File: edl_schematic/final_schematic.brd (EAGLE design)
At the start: 329.6 x 243.8 mm, 296 parts, among them IC1 FT232RL, IC14 TL084D, IC15 TL084D, IC16 TL084D, IC17 TL084D, IC18 TL084D, IC19 TL084D, IC20 TL084D, IC21 TL084D, IC22 TL084D, IC23 TL084D, IC24 TL084D, IC25 TL084D, IC26 TL084D, IC27 TL084D, IC28 TL084D, IC29 TL084D, IC3 TL084D, IC30 TL084D, IC4 TPS77333, IC5 TL084D, IC6 7812TV, Q1 BC558B, U1 TMS320F28069_PN_80, U3 TLV5610_DW_20, U4 MAX395EWG, U6 MAX395EWG, U7 MAX395EWG, X1 USB

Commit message: USB_UPDATED
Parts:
- removed X1: USB, con-berg:PN61729
- added CON1: UBC05V128-B0C04D, con-cypressindustries:32005-201
- added F1: 500mA, rcl:L1812
- added R19: 0, rcl:R1206
- added R20: 0, rcl:R1206W
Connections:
- new net N$12: CON1.2, R19.1
- new net N$13: CON1.3, R20.1
- new net XUSB: CON1.1, F1.2
- net GND: now also CON1.5; no longer X1.4
- net USBDM: now also R19.2; no longer X1.2
- net USBDP: now also R20.2; no longer X1.3
- net VBUS: now also F1.1; no longer X1.1
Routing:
- net USBDM: track 68.6 -> 89.6 mm, vias 0 -> 1
- net USBDP: track 78.6 -> 96.0 mm, vias 0 -> 1
- net N$13: track 0.00 -> 16.8 mm
- net N$12: track 0.00 -> 12.5 mm
- net XUSB: track 0.00 -> 11.5 mm
- net VBUS: track 110.9 -> 115.2 mm
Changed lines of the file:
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@@
 <attribute name="VALUE" x="82.130903125" y="62.0903" size="1.27" layer="27" rot="R270"/>
 </element>
-<element name="X1" library="con-berg" package="PN61729" value="USB" x="-30.1523375" y="47.800259375" smashed="yes" rot="R270">
-<attribute name="MF" value="" x="-11.694159375" y="63.14948125" size="1.778" layer="27" rot="R270" display="off"/>
-<attribute name="MPN" value="" x="-11.694159375" y="63.14948125" size="1.778" layer="27" rot="R270" display="off"/>
-<attribute name="NAME" x="-23.8023375" y="54.150259375" size="1.27" layer="25" rot="R270"/>
-<attribute name="OC_FARNELL" value="unknown" x="-11.694159375" y="63.14948125" size="1.778" layer="27" rot="R270" display="off"/>
-<attribute name="OC_NEWARK" value="unknown" x="-11.694159375" y="63.14948125" size="1.778" layer="27" rot="R270" display="off"/>
-<attribute name="VALUE" x="-39.0423375" y="40.180259375" size="1.27" layer="27"/>
+<element name="CON1" library="con-cypressindustries" package="32005-201" value="UBC05V128-B0C04D" x="-25.18155625" y="31.861759375" smashed="yes">
+<attribute name="MF" value="" x="-35.8038375" y="46.898559375" size="1.778" layer="27" display="off"/>
+<attribute name="MPN" value="" x="-35.8038375" y="46.898559375" size="1.778" layer="27" display="off"/>
+<attribute name="NAME" x="-29.62655625" y="37.576759375" size="1.27" layer="25"/>
+<attribute name="OC_FARNELL" value="unknown" x="-35.8038375" y="46.898559375" size="1.778" layer="27" display="off"/>
+<attribute name="OC_NEWARK" value="unknown" x="-35.8038375" y="46.898559375" size="1.778" layer="27" display="off"/>
+<attribute name="VALUE" x="-29.62655625" y="24.876759375" size="1.27" layer="27"/>
+</element>
+<element name="F1" library="rcl" package="L1812" value="500mA" x="-11.932921875" y="36.3245375" smashed="yes" rot="R180">
+<attribute name="NAME" x="-10.027921875" y="34.4195375" size="1.27" layer="25" rot="R180"/>
+<attribute name="VALUE" x="-10.027921875" y="39.4995375" size="1.27" layer="27" rot="R180"/>
+</element>
+<element name="R19" library="rcl" package="R1206" value="0" x="-11.8516375" y="29.05251875" smashed="yes">
+<attribute name="NAME" x="-13.1216375" y="30.32251875" size="1.27" layer="25"/>
+<attribute name="VALUE" x="-13.1216375" y="26.51251875" size="1.27" layer="27"/>
+</element>
+<element name="R20" library="rcl" package="R1206W" value="0" x="-12.26311875" y="22.4028" smashed="yes">
+<attribute name="NAME" x="-14.16811875" y="23.6728" size="1.27" layer="25"/>
+<attribute name="VALUE" x="-14.16811875" y="19.8628" size="1.27" layer="27"/>
 </element>
 </elements>
@@
 <wire x1="17.7317375" y1="-42.367203125" x2="17.548859375" y2="-42.55008125" width="0.254" layer="1"/>
 <wire x1="11.793221875" y1="-80.39608125" x2="11.625578125" y2="-80.39608125" width="0.254" layer="1"/>
-<contactref element="X1" pad="4"/>
+<contactref element="CON1" pad="5"/>
 </signal>
 <signal name="VCC" class="1">
@@
 <contactref element="JP6" pad="1"/>
 <via x="1.457959375" y="60.03798125" extent="1-16" drill="0.35"/>
-<wire x1="5.255259375" y1="73.484740625" x2="5.255259375" y2="69.3521625" width="0.4064" layer="1"/>
+<wire x1="5.255259375" y1="73.484740625" x2="5.255259375" y2="71.224140625" width="0.4064" layer="1"/>
+<wire x1="5.255259375" y1="71.224140625" x2="5.255259375" y2="69.3521625" width="0.4064" layer="1"/>
 <wire x1="5.255259375" y1="69.3521625" x2="1.457959375" y2="65.5548625" width="0.4064" layer="1"/>
 <wire x1="1.457959375" y1="60.03798125" x2="1.457959375" y2="65.5548625" width="0.4064" layer="1"/>
 <wire x1="5.255259375" y1="73.484740625" x2="5.08" y2="73.66" width="0.4064" layer="1"/>
-<contactref element="X1" pad="1"/>
-<wire x1="13.84" y1="53.34" x2="12.23518125" y2="53.34" width="0.4064" layer="16"/>
-<wire x1="12.23518125" y1="53.34" x2="8.69188125" y2="56.8833" width="0.4064" layer="16"/>
-<wire x1="8.69188125" y1="56.8833" x2="-8.3972375" y2="56.8833" width="0.4064" layer="16"/>
-<wire x1="-8.3972375" y1="56.8833" x2="-18.80361875" y2="46.47691875" width="0.4064" layer="16"/>
-<wire x1="-18.80361875" y1="46.47691875" x2="-25.368996875" y2="46.47691875" width="0.4064" layer="16"/>
-<wire x1="-25.368996875" y1="46.47691875" x2="-25.4423375" y2="46.550259375" width="0.4064" layer="16"/>
 <wire x1="13.84" y1="57.15" x2="13.218159375" y2="57.15" width="0.4064" layer="16"/>
 <wire x1="10.330178125" y1="60.03798125" x2="1.457959375" y2="60.03798125" width="0.4064" layer="16"/>
 <wire x1="13.218159375" y1="57.15" x2="10.330178125" y2="60.03798125" width="0.4064" layer="16"/>
+<contactref element="F1" pad="1"/>
+<wire x1="-9.982921875" y1="36.3245375" x2="-9.982921875" y2="64.96884375" width="0.4064" layer="1"/>
+<wire x1="-9.982921875" y1="64.96884375" x2="-10.005059375" y2="64.99098125" width="0.4064" layer="1"/>
+<wire x1="-9.982921875" y1="64.96884375" x2="-9.982921875" y2="69.836578125" width="0.4064" layer="1"/>
+<wire x1="-8.595359375" y1="71.224140625" x2="5.255259375" y2="71.224140625" width="0.4064" layer="1"/>
+<wire x1="-9.982921875" y1="69.836578125" x2="-8.595359375" y2="71.224140625" width="0.4064" layer="1"/>
 </signal>
 <signal name="USBDM">
@@
 <wire x1="18.4912" y1="54.71146875" x2="18.4912" y2="51.12445" width="0.4064" layer="16"/>
 <wire x1="18.4912" y1="51.12445" x2="17.428228125" y2="50.061478125" width="0.4064" layer="16"/>
-<contactref element="X1" pad="2"/>
 <wire x1="18.53" y1="62.740540625" x2="-8.26008125" y2="62.740540625" width="0.4064" layer="16"/>
-<wire x1="-21.9503625" y1="49.050259375" x2="-25.4423375" y2="49.050259375" width="0.4064" layer="16"/>
-<wire x1="-8.26008125" y1="62.740540625" x2="-21.9503625" y2="49.050259375" width="0.4064" layer="16"/>
+<contactref element="R19" pad="2"/>
+<wire x1="-8.26008125" y1="62.740540625" x2="-8.26008125" y2="45.989240625" width="0.4064" layer="16"/>
+<wire x1="-8.26008125" y1="45.989240625" x2="-2.694940625" y2="40.4241" width="0.4064" layer="16"/>
+<wire x1="-2.694940625" y1="40.4241" x2="-2.694940625" y2="29.199840625" width="0.4064" layer="16"/>
+<wire x1="-2.694940625" y1="29.199840625" x2="-2.631440625" y2="29.136340625" width="0.4064" layer="16"/>
+<wire x1="-2.631440625" y1="29.136340625" x2="-6.626859375" y2="29.136340625" width="0.4064" layer="16"/>
+<wire x1="-6.626859375" y1="29.136340625" x2="-6.72338125" y2="29.03981875" width="0.4064" layer="16"/>
+<via x="-6.72338125" y="29.03981875" extent="1-16" drill="0.35"/>
+<wire x1="-6.72338125" y1="29.03981875" x2="-10.4169375" y2="29.03981875" width="0.4064" layer="1"/>
+<wire x1="-10.4169375" y1="29.03981875" x2="-10.4296375" y2="29.05251875" width="0.4064" layer="1"/>
 </signal>
 <signal name="USBDP">
@@
 <wire x1="19.086871875" y1="49.9482" x2="19.09966875" y2="49.960996875" width="0.4064" layer="16"/>
 <wire x1="18.865" y1="49.9482" x2="18.865" y2="49.945" width="0.2032" layer="16"/>
-<contactref element="X1" pad="3"/>
-<wire x1="13.97" y1="65.91" x2="-10.582596875" y2="65.91" width="0.4064" layer="16"/>
-<wire x1="-10.582596875" y1="65.91" x2="-27.4423375" y2="49.050259375" width="0.4064" layer="16"/>
+<contactref element="R20" pad="2"/>
+<wire x1="13.97" y1="65.91" x2="-4.4353" y2="65.91" width="0.4064" layer="16"/>
+<wire x1="-4.4353" y1="65.91" x2="-4.445" y2="65.9003" width="0.4064" layer="16"/>
+<via x="-4.445" y="65.9003" extent="1-16" drill="0.35"/>
+<wire x1="-4.445" y1="65.9003" x2="-5.37971875" y2="64.96558125" width="0.4064" layer="1"/>
+<wire x1="-5.37971875" y1="64.96558125" x2="-5.37971875" y2="25.613359375" width="0.4064" layer="1"/>
+<wire x1="-5.37971875" y1="25.613359375" x2="-8.590278125" y2="22.4028" width="0.4064" layer="1"/>
+<wire x1="-8.590278125" y1="22.4028" x2="-10.76411875" y2="22.4028" width="0.4064" layer="1"/>
 </signal>
 <signal name="3V3OUT">
@@
 <wire x1="82.02629375" y1="66.54291875" x2="84.78265625" y2="69.29928125" width="0.2032" layer="1"/>
 </signal>
+<signal name="XUSB">
+<contactref element="CON1" pad="1"/>
+<contactref element="F1" pad="2"/>
+<wire x1="-22.18155625" y1="33.461759375" x2="-18.270421875" y2="33.461759375" width="0.4064" layer="1"/>
+<wire x1="-18.133059375" y1="33.599121875" x2="-18.133059375" y2="36.60901875" width="0.4064" layer="1"/>
+<wire x1="-18.133059375" y1="36.60901875" x2="-14.167403125" y2="36.60901875" width="0.4064" layer="1"/>
+<wire x1="-14.167403125" y1="36.60901875" x2="-13.882921875" y2="36.3245375" width="0.4064" layer="1"/>
+<wire x1="-18.270421875" y1="33.461759375" x2="-18.133059375" y2="33.599121875" width="0.4064" layer="1"/>
+</signal>
+<signal name="N$12">
+<contactref element="CON1" pad="2"/>
+<contactref element="R19" pad="1"/>
+<wire x1="-22.18155625" y1="32.661759375" x2="-13.319859375" y2="32.661759375" width="0.4064" layer="1"/>
+<wire x1="-13.319859375" y1="32.661759375" x2="-13.307059375" y2="32.674559375" width="0.4064" layer="1"/>
+<wire x1="-13.307059375" y1="32.674559375" x2="-13.2736375" y2="32.6411375" width="0.4064" layer="1"/>
+<wire x1="-13.2736375" y1="32.6411375" x2="-13.2736375" y2="29.05251875" width="0.4064" layer="1"/>
+</signal>
+<signal name="N$13">
+<contactref element="CON1" pad="3"/>
+<contactref element="R20" pad="1"/>
+<wire x1="-22.18155625" y1="31.861759375" x2="-17.64538125" y2="31.861759375" width="0.4064" layer="1"/>
+<wire x1="-17.64538125" y1="31.861759375" x2="-17.61998125" y2="31.887159375" width="0.4064" layer="1"/>
+<wire x1="-17.61998125" y1="31.887159375" x2="-17.287240625" y2="31.55441875" width="0.4064" layer="1"/>
+<wire x1="-17.287240625" y1="31.55441875" x2="-17.287240625" y2="23.954740625" width="0.4064" layer="1"/>
+<wire x1="-17.287240625" y1="23.954740625" x2="-15.314059375" y2="23.954740625" width="0.4064" layer="1"/>
+<wire x1="-15.314059375" y1="23.954740625" x2="-13.76211875" y2="22.4028" width="0.4064" layer="1"/>
+</signal>
 </signals>

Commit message: some small changes
written in my EDL book
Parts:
- removed D2: 1N4004, diode:DO41-10
- added D3: 1N4004, diode:DO41-10
- added F2: 500mA, SparkFun:PTC-1206
- added R21, R22, R23: (no value), rcl:R1206
- moved C4 3.96 mm to (15.3, 57.0)
- moved C3 3.06 mm to (15.3, 60.2)
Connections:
- new net N$14: JP2.1, R4.2
- new net N$15: C20.1, R21.2, U1.48, Y1.2
- new net N$16: R23.1, U1.37
- new net N$17: C3.1, F2.1
- net 3V3: now also R22.2, R23.2; no longer C7.1, U1.20, U1.37
- net N$1: now also C7.1, R22.1, U1.20; no longer C20.1, U1.48, Y1.2
- net N$18: now also R21.1
- net N$23: now also D3.A; no longer D2.C
- net VBUS: now also F2.2; no longer C3.1, R4.2
- net VIN-: now also D3.C; no longer D2.A
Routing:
- net N$14: track 0.00 -> 100.1 mm, vias 0 -> 3
- net N$15: track 0.00 -> 21.1 mm
- net VBUS: track 115.2 -> 94.4 mm
- net 3V3: track 1612.9 -> 1595.4 mm, vias 37 -> 35
- net N$23: track 28.4 -> 34.9 mm
- net N$1: track 18.2 -> 12.8 mm, vias 0 -> 2
- net N$17: track 0.00 -> 4.78 mm
- net VIN-: track 3.81 -> 8.12 mm
- net N$16: track 0.00 -> 2.98 mm
- net N$18: track 19.9 -> 21.9 mm

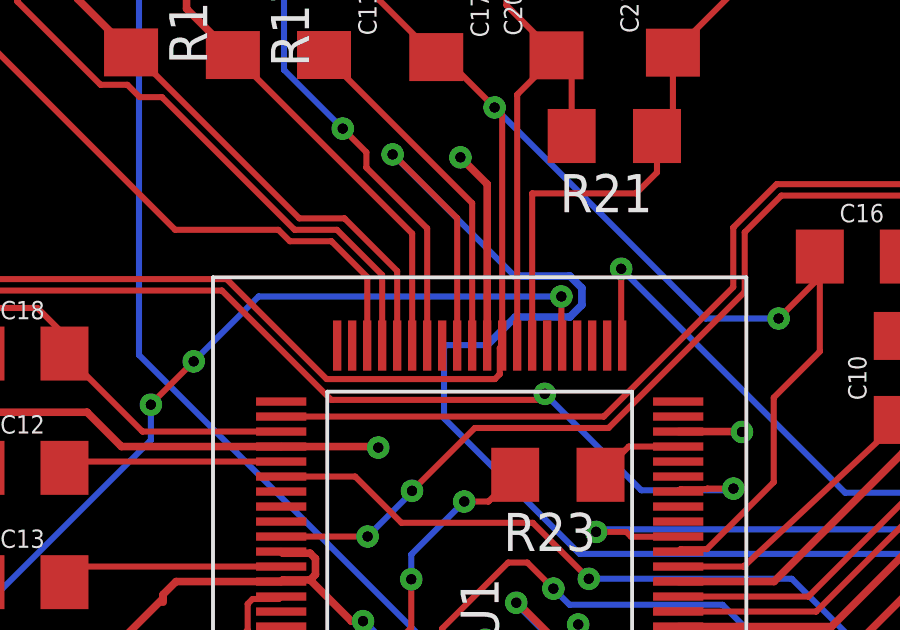
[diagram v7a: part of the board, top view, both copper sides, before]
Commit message: TXD connection changed
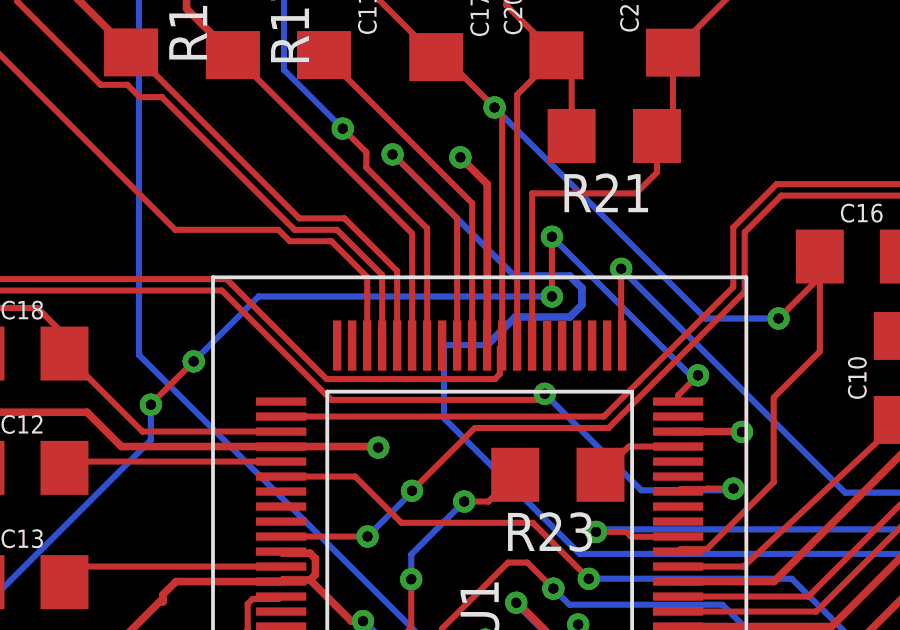
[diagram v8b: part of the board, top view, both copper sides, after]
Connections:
- net TXD: now also U1.40; no longer U1.45
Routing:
- net TXD: track 86.1 -> 93.9 mm, vias 5 -> 7
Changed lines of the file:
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@@
 <contactref element="IC1" pad="1"/>
 <contactref element="JP4" pad="3"/>
-<contactref element="U1" pad="45"/>
 <wire x1="5.08" y1="43.789596875" x2="7.455878125" y2="41.41371875" width="0.4064" layer="16"/>
 <wire x1="7.455878125" y1="41.41371875" x2="11.53371875" y2="41.41371875" width="0.4064" layer="16"/>
@@
 <wire x1="16.2941" y1="23.23338125" x2="35.326321875" y2="23.23338125" width="0.2032" layer="16"/>
 <via x="44.7421" y="33.830259375" extent="1-16" drill="0.35"/>
-<wire x1="58.39714375" y1="37.330378125" x2="58.42508125" y2="37.302440625" width="0.2032" layer="16"/>
-<wire x1="58.42508125" y1="37.302440625" x2="58.42508125" y2="37.437059375" width="0.2032" layer="16"/>
-<via x="58.42508125" y="37.437059375" extent="1-16" drill="0.35"/>
-<wire x1="58.42508125" y1="37.437059375" x2="58.42508125" y2="35.828415625" width="0.2032" layer="1"/>
-<wire x1="58.42508125" y1="35.828415625" x2="58.4522" y2="35.801296875" width="0.2032" layer="1"/>
 <wire x1="35.326321875" y1="23.23338125" x2="44.7421" y2="32.649159375" width="0.2032" layer="16"/>
 <wire x1="44.74971875" y1="33.837878125" x2="44.7421" y2="33.830259375" width="0.2032" layer="1"/>
 <wire x1="44.7421" y1="33.830259375" x2="44.7421" y2="32.649159375" width="0.2032" layer="16"/>
-<wire x1="58.42508125" y1="37.437059375" x2="48.333659375" y2="37.437059375" width="0.2032" layer="16"/>
-<wire x1="48.333659375" y1="37.437059375" x2="46.16958125" y2="35.27298125" width="0.2032" layer="16"/>
+<wire x1="46.16958125" y1="35.27298125" x2="48.333659375" y2="37.437059375" width="0.2032" layer="16"/>
 <via x="46.16958125" y="35.27298125" extent="1-16" drill="0.35"/>
 <wire x1="46.16958125" y1="35.27298125" x2="44.74971875" y2="33.85311875" width="0.2032" layer="1"/>
 <wire x1="44.74971875" y1="33.85311875" x2="44.74971875" y2="33.837878125" width="0.2032" layer="1"/>
+<contactref element="U1" pad="40"/>
+<wire x1="48.333659375" y1="37.437059375" x2="58.110115625" y2="37.437059375" width="0.2032" layer="16"/>
+<wire x1="58.110115625" y1="37.437059375" x2="58.11011875" y2="37.4370625" width="0.2032" layer="16"/>
+<via x="58.11011875" y="37.4370625" extent="1-16" drill="0.35"/>
+<wire x1="58.11011875" y1="37.4370625" x2="58.11011875" y2="39.42810625" width="0.2032" layer="1"/>
+<wire x1="58.11011875" y1="39.42810625" x2="58.10980625" y2="39.42841875" width="0.2032" layer="1"/>
+<via x="58.10980625" y="39.42841875" extent="1-16" drill="0.35"/>
+<wire x1="58.10980625" y1="39.42841875" x2="62.730065625" y2="34.808159375" width="0.2032" layer="16"/>
+<wire x1="62.730065625" y1="34.808159375" x2="62.9793" y2="34.808159375" width="0.2032" layer="16"/>
+<via x="62.9793" y="34.808159375" extent="1-16" drill="0.35"/>
+<wire x1="62.9793" y1="34.808159375" x2="62.3189" y2="34.147759375" width="0.2032" layer="1"/>
+<wire x1="62.3189" y1="34.147759375" x2="62.3189" y2="33.934596875" width="0.2032" layer="1"/>
 </signal>
 <signal name="N$4">
